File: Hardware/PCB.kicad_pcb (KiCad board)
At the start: 2 copper layers, 55.4 x 21.2 mm, 15 parts, among them J2 Conn_01x06, SW1 TS04-66-43-BK-100-SMT, U1 ME54BS01_V1.0, U3 MCP1700x-330xxTT

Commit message: WIP
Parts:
- removed the D1 at (54.0, 71.8)
- removed the R3 at (54.9, 74.8)
- removed SW1: TS04-66-43-BK-100-SMT, TS04-66-43-BK-100-SMT:SW_TS04-66-43-BK-100-SMT
- added C3: C, Capacitor_SMD:C_0805_2012Metric, F.Cu at (42.7, 89.5)
- added Q1: Q_NMOS, Package_TO_SOT_SMD:SOT-23, F.Cu at (43.0, 85.7)
- added R4: 100K, Resistor_SMD:R_0805_2012Metric_Pad1.20x1.40mm_HandSolder, F.Cu at (57.2, 96.0)
- added R5: 100K, Resistor_SMD:R_0805_2012Metric_Pad1.20x1.40mm_HandSolder, F.Cu at (57.2, 98.9)
- added R6: 1M, Resistor_SMD:R_0805_2012Metric, F.Cu at (47.2, 89.4)
- added SW2: SW_Push, Button_Switch_SMD:SW_SPST_TS-1088-xR025, F.Cu at (46.5, 113.5)
- Batt1: footprint S2B-PH-SM4-TB:JST_S2B-PH-SM4-TB -> Battery:BatteryHolder_Keystone_3034_1x20mm
- Probe1, Probe2: footprint S2B-PH-SM4-TB:JST_S2B-PH-SM4-TB -> Connector_JST:JST_PH_B2B-PH-SM4-TB_1x02-1MP_P2.00mm_Vertical
- R3: value 50 -> 5K1
- moved R3 44.4 mm to (53.0, 77.0)
- moved D1 44.1 mm to (53.0, 74.5)
- moved Batt1 10.1 mm to (38.0, 67.5)
- moved C1 5.39 mm to (48.5, 58.0), turned to 90 degrees
- moved U3 4.66 mm to (52.0, 59.0)
- moved Probe2 3.44 mm to (71.5, 60.0)
- moved Probe1 3.14 mm to (61.7, 60.2)
- moved C2 2.09 mm to (55.5, 58.0), turned to 90 degrees
- moved U1 1.21 mm to (85.7, 67.6)
- moved R2 0.29 mm to (73.5, 67.0), turned to 0 degrees
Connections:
- net Net-(Batt1-Pin_1) renamed +BATT
- net Net-(J2-Pin_2) renamed NRESET
- net Net-(J2-Pin_3) renamed SWDIO
- net Net-(J2-Pin_4) renamed SWDCLK
- net Net-(J2-Pin_5) renamed +1V8
- net Net-(Probe1-Pin_2) renamed PROBE_1_DIVIDER
- net Net-(Probe2-Pin_1) renamed PROBE_2_DIVIDER
- net Net-(U1-P1.09) renamed PROBE_1_PWR
- net Net-(U1-P1.10) renamed PROBE_2_PWR
- Batt1 pad 2: GND -> -BATT
- U1 pad 21: Net-(U1-P2.09) -> unconnected-(U1-P2.09-Pad21)
- U1 pad 6: unconnected-(U1-P1.13/AIN6-Pad6) -> BUTTON
- U1 pad 7: unconnected-(U1-P1.14/AIN7-Pad7) -> BATT_M
- U1 pad 8: unconnected-(U1-P1.06/AIN2-Pad8) -> BATT_M
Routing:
- net Net-(U1-P2.09): track 54.4 -> 0.00 mm, vias 2 -> 0
- net +1V8: track 53.5 -> 0.00 mm
- net Net-(U1-P2.10): track 35.8 -> 0.00 mm
- net LED: track 0.00 -> 34.2 mm
- net PROBE_1_DIVIDER: track 37.0 -> 7.01 mm
- net GND: track 25.2 -> 0.00 mm, vias 7 -> 0
- net PROBE_2_PWR: track 21.6 -> 0.00 mm
- net +BATT: track 25.4 -> 8.03 mm
- net PROBE_2_DIVIDER: track 23.9 -> 40.6 mm
- net PROBE_1_PWR: track 34.9 -> 32.1 mm
- net Net-(D1-A): track 2.16 -> 0.00 mm
- net -BATT: vias 0 -> 2
- added copper zone on F.Cu, net GND
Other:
- board size 55.4 x 21.2 mm -> 67.5 x 24.2 mm
- board text added: "@tomasmcguinness Dual Temperature Sensor nRF54L15 REVISION ${REVISION}"
- board text added: "CA9M7"
- board text removed: "@tomasmcguinness Dual Temperature Sensor nRF54L15 v${REVISION}"
- board text removed: "CA8M6"

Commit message: WIP
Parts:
- added C4: 100nF, Capacitor_SMD:C_0805_2012Metric, F.Cu at (73.5, 67.0)
- added C5: 100nF, Capacitor_SMD:C_0805_2012Metric, F.Cu at (63.5, 65.0)
- C3: value C -> 100nF
- R1: footprint Resistor_SMD:R_0805_2012Metric_Pad1.20x1.40mm_HandSolder -> Resistor_SMD:R_0805_2012Metric
- moved SW2 45.2 mm to (62.0, 71.0)
- moved R5 32.5 mm to (55.5, 66.5)
- moved R4 32.0 mm to (55.5, 64.0), turned to 180 degrees
- moved C3 24.5 mm to (57.0, 69.5), turned to -90 degrees
- moved Q1 22.2 mm to (51.0, 65.0), turned to 180 degrees
- moved R6 21.0 mm to (52.0, 69.0), turned to -90 degrees
- moved J2 2.97 mm to (73.7, 77.0)
- moved D1 2.83 mm to (51.0, 76.5)
- moved R1 2.13 mm to (63.5, 67.0)
- moved R3 2.06 mm to (55.0, 76.5), turned to 180 degrees
- moved R2 2.00 mm to (73.5, 69.0), turned to 180 degrees
- moved Probe2 0.25 mm to (71.5, 60.2)
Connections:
- Batt1 pad 2: -BATT -> GND
- Probe2 pad 1: PROBE_2_DIVIDER -> GND
- Probe2 pad 2: GND -> PROBE_2_DIVIDER
- Q1 pad 1: (no net) -> BATT_M_CTRL
- Q1 pad 2: (no net) -> Net-(Q1-PadG)
- Q1 pad 3: (no net) -> +BATT
- R4 pad 2: Net-(Q1-PadS) -> Net-(Q1-PadG)
- U1 pad 7: BATT_M -> BATT_M_CTRL
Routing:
- net +1V8: track 0.00 -> 49.7 mm, vias 0 -> 2
- net +BATT: track 8.03 -> 51.9 mm
- net BATT_M_CTRL: track 0.00 -> 42.0 mm, vias 0 -> 2
- net BATT_M: track 0.00 -> 38.4 mm, vias 0 -> 2
- net PROBE_1_DIVIDER: track 7.01 -> 37.5 mm
- net BUTTON: track 0.00 -> 29.3 mm, vias 0 -> 2
- net PROBE_2_PWR: track 0.00 -> 20.6 mm
- net PROBE_2_DIVIDER: track 40.6 -> 26.8 mm
- net Net-(Q1-PadG): track 0.00 -> 3.08 mm
- net PROBE_1_PWR: track 32.1 -> 34.5 mm
- net Net-(D1-A): track 0.00 -> 2.15 mm
- net GND: track 0.00 -> 1.82 mm, vias 0 -> 5
- net SWDIO: track 26.1 -> 27.5 mm
- net SWDCLK: track 29.4 -> 30.5 mm
- net LED: track 34.2 -> 33.3 mm
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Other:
- board text removed: "+"

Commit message: WIP
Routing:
- net BATT_M: track 38.4 -> 37.6 mm
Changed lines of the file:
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@@
 	)
 	(segment
-		(start 59 66)
-		(end 80 66)
-		(width 0.25)
-		(layer "B.Cu")
-		(net "BATT_M")
-	)
-	(segment
-		(start 85.071 60.568227)
-		(end 85.114227 60.525)
-		(width 0.25)
-		(layer "B.Cu")
-		(net "BATT_M")
-	)
-	(segment
-		(start 80 66)
-		(end 85.071 60.929)
+		(start 58 65)
+		(end 81 65)
 		(width 0.25)
 		(layer "B.Cu")
@@
 	)
 	(segment
-		(start 58 65)
-		(end 59 66)
+		(start 81 65)
+		(end 85.071 60.929)
 		(width 0.25)
 		(layer "B.Cu")
+		(net "BATT_M")
+	)
+	(segment
+		(start 85.071 60.568227)
+		(end 85.114227 60.525)
+		(width 0.25)
+		(layer "B.Cu")

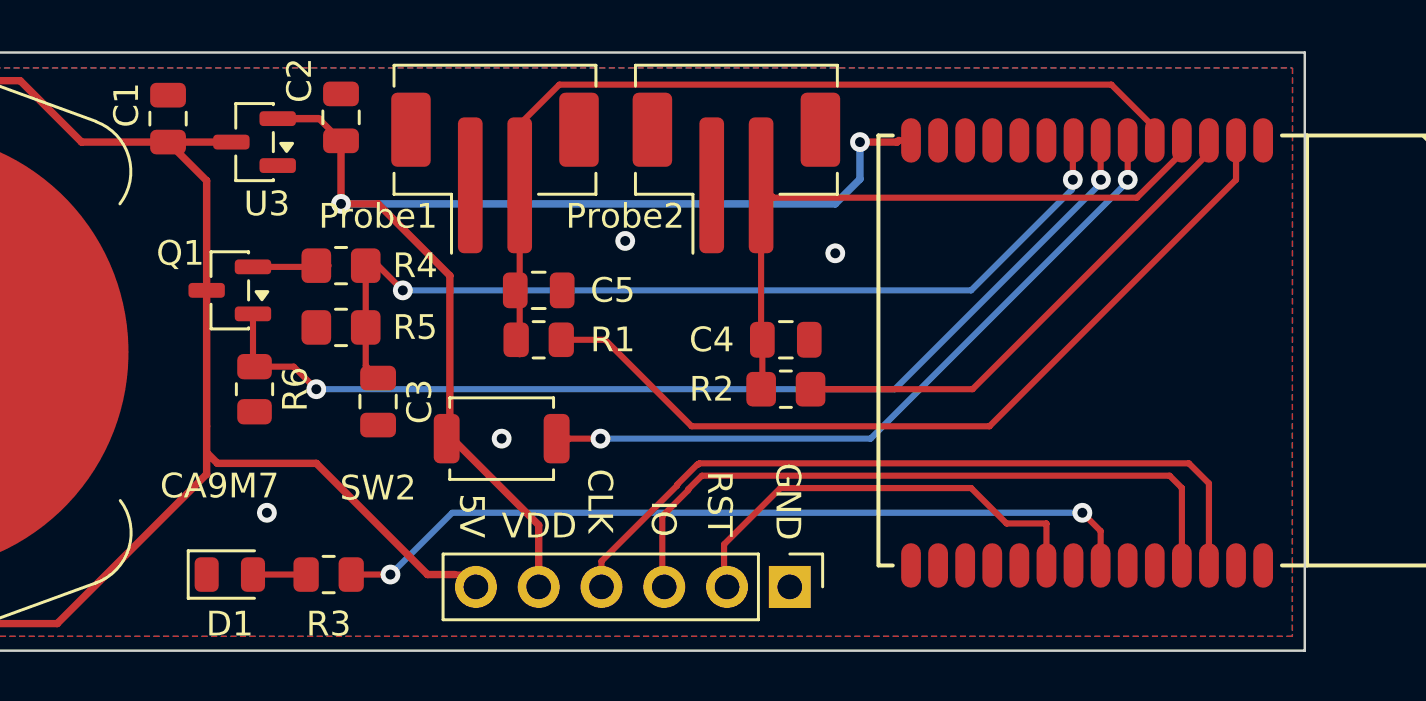
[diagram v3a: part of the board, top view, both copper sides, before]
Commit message: WIP Finished outline with LDO
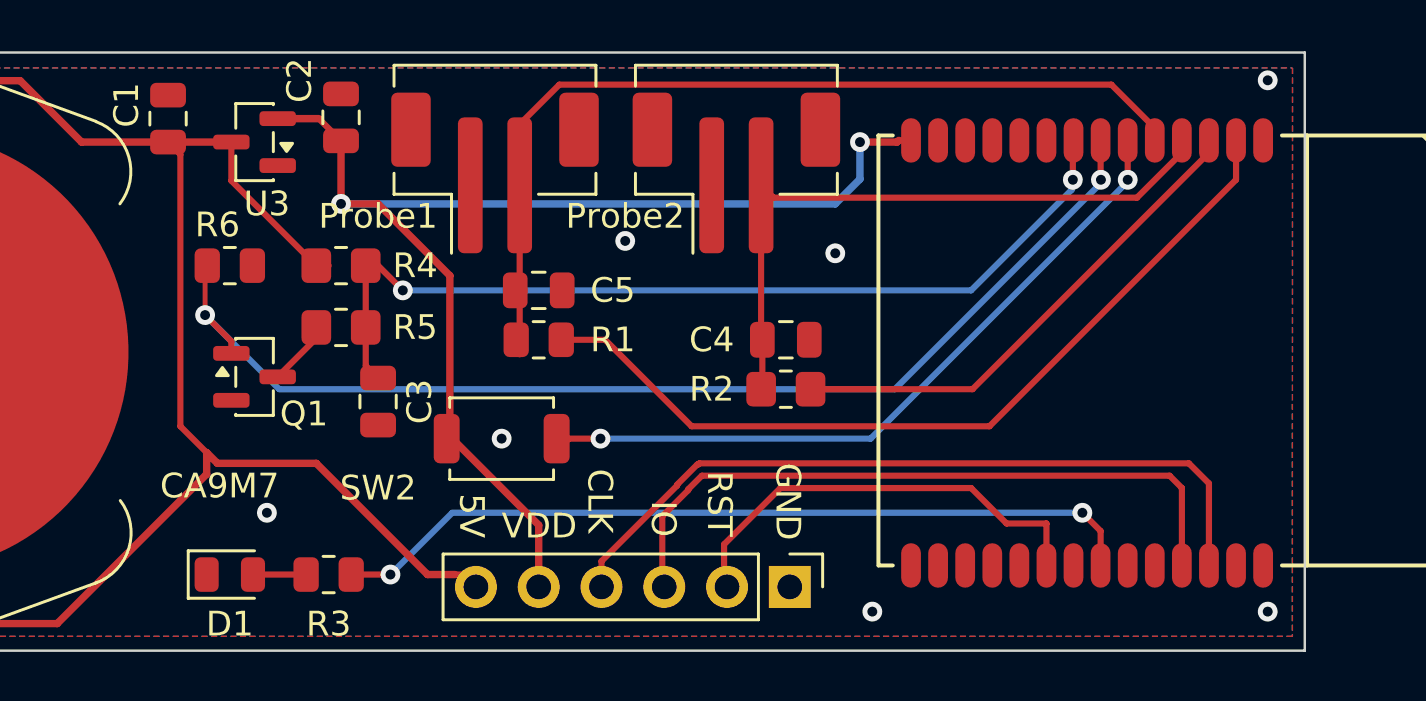
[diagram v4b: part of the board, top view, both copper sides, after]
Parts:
- U3: value MCP1700x-330xxTT -> MCP1700x-180xxTT
- moved R6 5.10 mm to (51.0, 64.0), turned to 0 degrees
- moved Q1 3.64 mm to (52.0, 68.5), turned to 0 degrees
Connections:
- Q1 pad 2: Net-(Q1-PadG) -> GND
- Q1 pad 3: +BATT -> Net-(Q1-D)
- R4 pad 2: Net-(Q1-PadG) -> +BATT
- R5 pad 1: GND -> Net-(Q1-D)
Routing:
- net +BATT: track 51.9 -> 58.4 mm
- net Net-(Q1-PadG): track 3.08 -> 0.00 mm
- net BATT_M_CTRL: track 42.0 -> 44.7 mm
- net Net-(Q1-D): track 0.00 -> 2.65 mm
- net GND: vias 5 -> 8
